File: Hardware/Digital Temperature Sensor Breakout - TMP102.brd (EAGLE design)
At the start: 15.2 x 15.2 mm, 13 parts, among them U1 TMP102-1:1

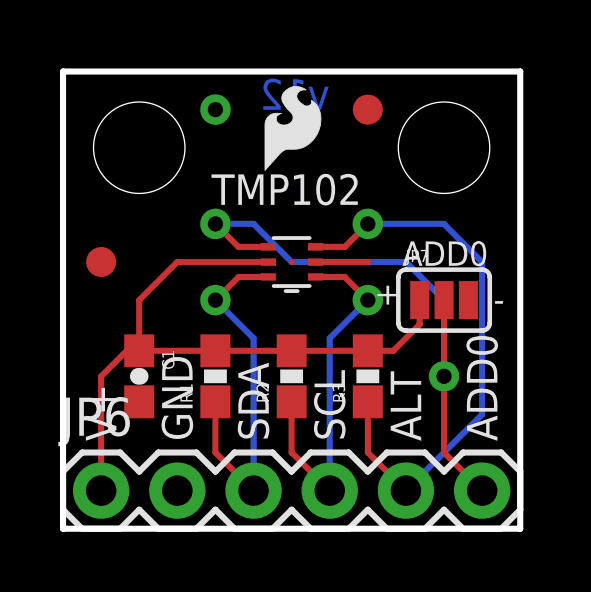
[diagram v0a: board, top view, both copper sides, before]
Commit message: Renamed board files
Renamed board files to match name of product on storefront. Also,
replaced main IC device with properly named variant from updated library
on github.
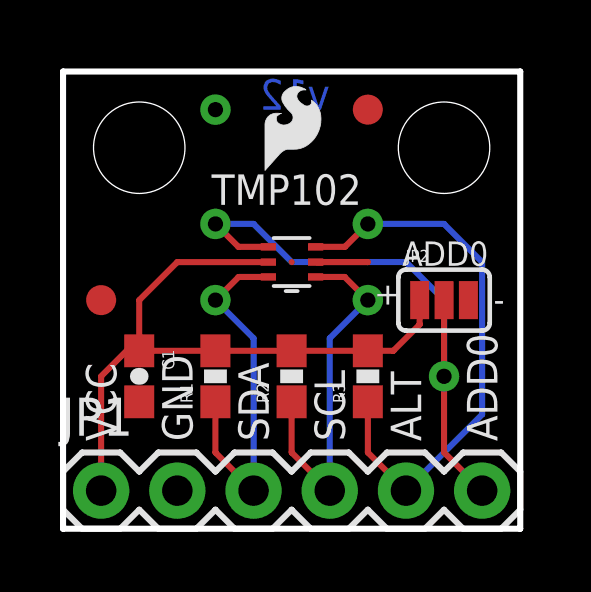
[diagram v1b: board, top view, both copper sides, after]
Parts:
- JP1: value STAND-OFFTIGHT -> (none); device SparkFun:STAND-OFF-TIGHT -> SparkFun:1X06
- JP2: value STAND-OFFTIGHT -> JUMPER-32-3; device SparkFun:STAND-OFF-TIGHT -> SparkFun:SJ_3_PASTE2&3
- JP6: value (none) -> STAND-OFFTIGHT; device SparkFun:1X06 -> SparkFun:STAND-OFF-TIGHT
- JP7: value JUMPER-32-3 -> STAND-OFFTIGHT; device SparkFun:SJ_3_PASTE2&3 -> SparkFun:STAND-OFF-TIGHT
- U1: value TMP102-1:1 -> TMP1021:1; device SparkFun:SOT563-2 -> SparkFun-Sensors:SOT563-2
- moved JP1 11.5 mm to (1.27, 1.27)
- moved JP6 11.5 mm to (2.54, 12.7)
- moved JP2 5.08 mm to (12.7, 7.62)
- moved JP7 5.08 mm to (12.7, 12.7)
- moved JP4 1.27 mm to (1.27, 7.62)
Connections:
- removed net V+: C1.1, JP6.1, JP7.1, R1.2, R2.2, R3.2, U1.5
- new net VCC: C1.1, JP1.1, JP2.1, R1.2, R2.2, R3.2, U1.5
- net ADD0: now also JP1.6, JP2.2; no longer JP6.6, JP7.2
- net ALERT: now also JP1.5; no longer JP6.5
- net GND: now also JP1.2, JP2.3; no longer JP6.2, JP7.3
- net SCL: now also JP1.4; no longer JP6.4
- net SDA: now also JP1.3; no longer JP6.3
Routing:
- net VCC: track 0.00 -> 22.5 mm
- net V+: track 22.5 -> 0.00 mm
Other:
- board text added: "VCC"
- board text removed: "V+"
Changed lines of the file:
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@@
 <text x="10.922" y="2.921" size="1.016" layer="22" font="vector" ratio="15" rot="MR90">ALT</text>
 <text x="5.842" y="2.921" size="1.016" layer="22" font="vector" ratio="15" rot="MR90">SDA</text>
-<text x="0.762" y="2.921" size="1.016" layer="22" font="vector" ratio="15" rot="MR90">V+</text>
+<text x="0.762" y="2.921" size="1.016" layer="22" font="vector" ratio="15" rot="MR90">VCC</text>
 <text x="13.462" y="2.921" size="1.016" layer="22" font="vector" ratio="15" rot="MR90">ADD0</text>
 <text x="4.953" y="10.795" size="1.016" layer="21" ratio="15">TMP102</text>
-<text x="8.89" y="13.97" size="1.016" layer="16" font="vector" ratio="15" rot="MR0">v12</text>
+<text x="8.89" y="13.97" size="1.016" layer="16" font="vector" ratio="20" rot="MR0">v12</text>
 <text x="11.176" y="7.366" size="0.8128" layer="21" font="vector" ratio="15" rot="R90">+</text>
 <text x="14.351" y="7.239" size="0.8128" layer="21" font="vector" ratio="15">-</text>
@@
 <text x="11.938" y="2.921" size="1.016" layer="21" font="vector" ratio="15" rot="R90">ALT</text>
 <text x="6.858" y="2.921" size="1.016" layer="21" font="vector" ratio="15" rot="R90">SDA</text>
-<text x="1.778" y="2.921" size="1.016" layer="21" font="vector" ratio="15" rot="R90">V+</text>
+<text x="1.778" y="2.921" size="1.016" layer="21" font="vector" ratio="15" rot="R90">VCC</text>
 <text x="14.478" y="2.921" size="1.016" layer="21" font="vector" ratio="15" rot="R90">ADD0</text>
 <text x="11.303" y="8.763" size="0.8128" layer="21" font="vector" ratio="15">ADD0</text>
@@
 <element name="C1" library="SparkFun" package="0603-CAP" value="0.1uF" x="2.54" y="5.08" rot="R270"/>
 <element name="JP3" library="SparkFun" package="SFE-LOGO-FLAME" value="LOGO-SFESK" x="6.731" y="11.938"/>
-<element name="JP4" library="SparkFun" package="FIDUCIAL-1X2" value="FIDUCIAL1X2" x="1.27" y="8.89"/>
+<element name="JP4" library="SparkFun" package="FIDUCIAL-1X2" value="FIDUCIAL1X2" x="1.27" y="7.62"/>
 <element name="JP5" library="SparkFun" package="FIDUCIAL-1X2" value="FIDUCIAL1X2" x="10.16" y="13.97"/>
-<element name="JP6" library="SparkFun" package="1X06" value="" x="1.27" y="1.27"/>
-<element name="JP1" library="SparkFun" package="STAND-OFF-TIGHT" value="STAND-OFFTIGHT" x="2.54" y="12.7"/>
-<element name="JP2" library="SparkFun" package="STAND-OFF-TIGHT" value="STAND-OFFTIGHT" x="12.7" y="12.7"/>
-<element name="JP7" library="SparkFun" package="SJ_3_PASTE2&amp;3" value="JUMPER-32-3" x="12.7" y="7.62"/>
-<element name="U1" library="SparkFun" package="SOT563-2" value="TMP102-1:1" x="7.62" y="8.89" rot="R180"/>
+<element name="JP1" library="SparkFun" package="1X06" value="" x="1.27" y="1.27"/>
+<element name="JP2" library="SparkFun" package="SJ_3_PASTE2&amp;3" value="JUMPER-32-3" x="12.7" y="7.62"/>
+<element name="U1" library="SparkFun-Sensors" package="SOT563-2" value="TMP1021:1" x="7.62" y="8.89" rot="R180"/>
 <element name="U$1" library="SparkFun" package="OSHW-LOGO-S" value="" x="7.62" y="8.89" rot="MR0"/>
+<element name="JP6" library="SparkFun" package="STAND-OFF-TIGHT" value="STAND-OFFTIGHT" x="2.54" y="12.7"/>
+<element name="JP7" library="SparkFun" package="STAND-OFF-TIGHT" value="STAND-OFFTIGHT" x="12.7" y="12.7"/>
 </elements>
 <signals>
@@
 <vertex x="0" y="0"/>
 </polygon>
-<contactref element="JP6" pad="2"/>
-<contactref element="JP7" pad="3"/>
+<contactref element="JP1" pad="2"/>
+<contactref element="JP2" pad="3"/>
 <contactref element="U1" pad="2"/>
 <polygon width="0.254" layer="1" isolate="0.3048">
@@
 </signal>
 <signal name="SCL">
-<contactref element="JP6" pad="4"/>
+<contactref element="JP1" pad="4"/>
 <contactref element="U1" pad="1"/>
 <contactref element="R2" pad="1"/>
@@
 </signal>
 <signal name="ALERT">
-<contactref element="JP6" pad="5"/>
+<contactref element="JP1" pad="5"/>
 <contactref element="U1" pad="3"/>
 <contactref element="R3" pad="1"/>
@@
 </signal>
 <signal name="SDA">
-<contactref element="JP6" pad="3"/>
+<contactref element="JP1" pad="3"/>
 <contactref element="U1" pad="6"/>
 <contactref element="R1" pad="1"/>
@@
 </signal>
 <signal name="ADD0">
-<contactref element="JP6" pad="6"/>
-<contactref element="JP7" pad="2"/>
+<contactref element="JP1" pad="6"/>
+<contactref element="JP2" pad="2"/>
 <contactref element="U1" pad="4"/>
 <wire x1="12.7" y1="2.54" x2="13.97" y2="1.27" width="0.2032" layer="1"/>
@@
 <wire x1="12.7" y1="2.54" x2="12.7" y2="5.08" width="0.2032" layer="1"/>
 </signal>
-<signal name="V+">
-<contactref element="JP6" pad="1"/>
-<contactref element="JP7" pad="1"/>
+<signal name="VCC">
+<contactref element="JP1" pad="1"/>
+<contactref element="JP2" pad="1"/>
 <contactref element="R3" pad="2"/>
 <contactref element="R2" pad="2"/>
@@
 </signal>
 </signals>
+<errors>
+</errors>
 </board>
 </drawing>

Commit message: Added better info in schematic
Added a change log, version number, default i2c address info, and
creative commons note to schematic.
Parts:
- added U$2: CREATIVE_COMMONS, SparkFun:CREATIVE_COMMONS
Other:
- board text added: "Kade Alexander Jensen"

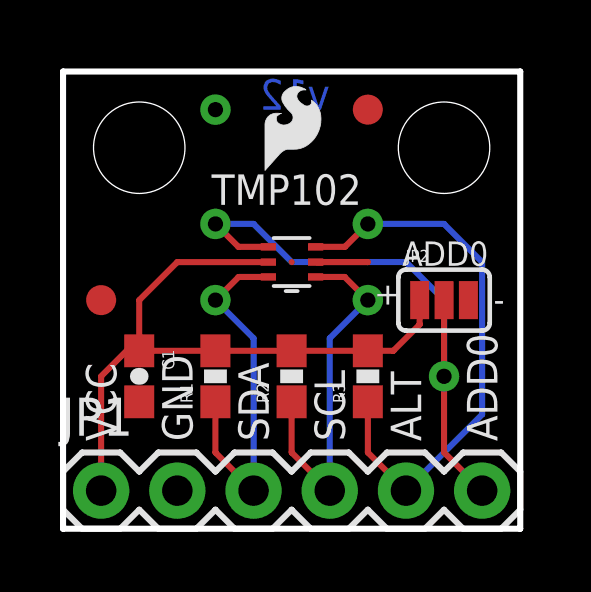
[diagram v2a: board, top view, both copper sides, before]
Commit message: Revision 13 changes
-Changed I2C address from 0x90 to 0x48.
-Changed I2C pull-up values to 4.7k
-Changed Alert pin pull-up to 4.7k
-Added I2C pull-up solder jumper
-Changed ADD0 pull-down jumper to 2-pad NC
-Added table of I2C addresses based on ADD0 connection.
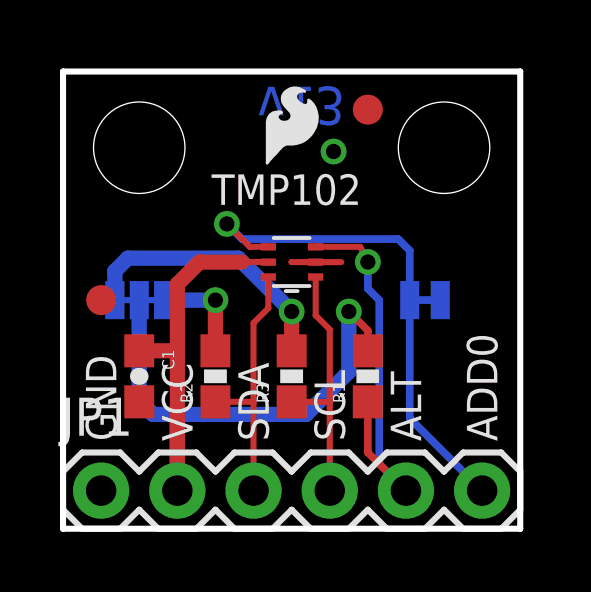
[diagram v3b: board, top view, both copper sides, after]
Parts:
- removed JP4: FIDUCIAL1X2, SparkFun:FIDUCIAL-1X2
- removed U$1: (no value), SparkFun:OSHW-LOGO-S
- added FRAME2: (no value), SparkFun-Aesthetics:CREATIVE_COMMONS
- added JP8: STAND-OFFTIGHT, SparkFun:STAND-OFF-TIGHT
- added LOGO2: SFE_LOGO_FLAME.1_INCH, SparkFun-Aesthetics:SFE_LOGO_FLAME_.1
- added LOGO3: OSHW-LOGOS, SparkFun-Aesthetics:OSHW-LOGO-S
- JP2: value JUMPER-32-3 -> (none); device SparkFun:SJ_3_PASTE2&3 -> SparkFun-Passives:PAD-JUMPER-3-3OF3_NC_BY_TRACE_YES_SILK_FULL_BOX
- JP3: value LOGO-SFESK -> ADD0; device SparkFun:SFE-LOGO-FLAME -> SparkFun-Passives:PAD-JUMPER-2-NC_BY_TRACE_YES_SILK
- JP6: value STAND-OFFTIGHT -> FIDUCIAL1X2; device SparkFun:STAND-OFF-TIGHT -> SparkFun:FIDUCIAL-1X2
- R1, R2, R3: value 1K -> 4.7k
- U$2: value CREATIVE_COMMONS -> REVISION; device SparkFun:CREATIVE_COMMONS -> SparkFun-Aesthetics:REVISION
- moved U$2 21.5 mm to (-10.8, -25.4)
- moved JP5 10.9 mm to (1.27, 7.62)
- moved JP2 10.2 mm to (2.54, 7.62), flipped to the bottom, turned to 180 degrees
- moved JP7 10.2 mm to (2.54, 12.7)
- moved JP6 7.73 mm to (10.2, 14.0)
- moved JP3 6.86 mm to (12.1, 7.62), flipped to the bottom, turned to 180 degrees
- moved R1 5.08 mm to (10.2, 5.08)
- moved R2 2.54 mm to (5.08, 5.08)
- moved R3 2.54 mm to (7.62, 5.08)
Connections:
- new net N$1: JP2.1, R3.2
- new net N$2: JP2.3, R2.2
- net ADD0: now also JP3.1; no longer JP2.2
- net ALERT: now also R1.1; no longer R3.1
- net GND: now also JP1.1, JP3.2; no longer JP1.2, JP2.3
- net SCL: now also R3.1; no longer R2.1
- net SDA: now also R2.1; no longer R1.1
- net VCC: now also JP1.2, JP2.2; no longer JP1.1, JP2.1, R2.2, R3.2
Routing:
- net N$1: track 0.00 -> 9.08 mm, vias 0 -> 1
- net VCC: track 22.5 -> 28.8 mm, vias 0 -> 1
- net ALERT: track 18.6 -> 13.7 mm
- net SDA: track 12.4 -> 8.60 mm, vias 1 -> 0
- net SCL: track 12.4 -> 8.59 mm, vias 1 -> 0
- net N$2: track 0.00 -> 3.42 mm, vias 0 -> 1
- net ADD0: track 20.2 -> 17.2 mm, vias 2 -> 1
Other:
- board text added: "Alex Wende"
- board text added: "I2C PU"
- board text removed: "+"
- board text removed: "v12"

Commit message: Applied Fixes from Design Review
-Moved traces on end of sensors to extend out the other way.
-Added note in schematic about using an external jumper to change I2C
address.
-Removed Kade's name from document layer.
-Added pull down resistor to prevent shorts with I2C address changes.
-Added unit of measurement on Measures layer.
-Changed measurements to use 0,0 as reference.
-Removed "-" on ADD0 jumper
-Changed VCC silk on top silk to voltage range.
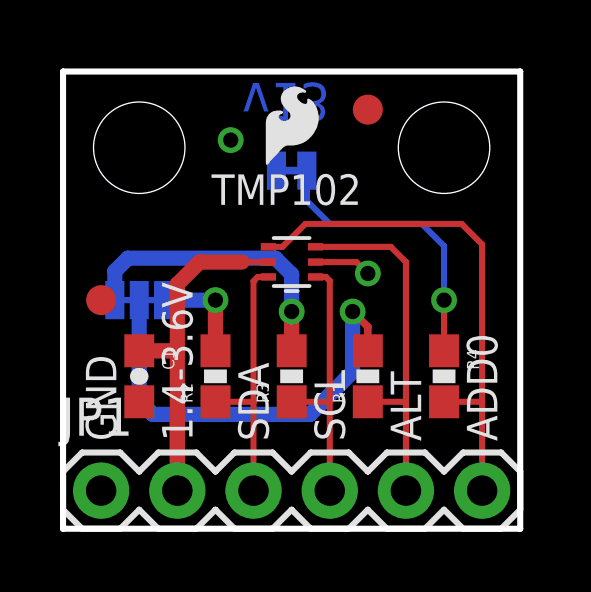
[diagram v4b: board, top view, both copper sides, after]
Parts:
- added R4: 10k, SparkFun:0603-RES
- R1: value 4.7k -> 10k
- moved JP3 6.20 mm to (7.62, 11.9), turned to 0 degrees
- moved LOGO3 5.09 mm to (12.7, 9.27)
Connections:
- new net N$3: JP3.1, R4.1
- net ADD0: now also R4.2; no longer JP3.1
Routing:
- net N$3: track 0.00 -> 9.70 mm, vias 0 -> 1
- net ALERT: track 13.7 -> 12.1 mm, vias 1 -> 0
- net N$1: track 9.08 -> 9.81 mm
- net GND: track 1.67 -> 1.90 mm, vias 1 -> 2
- net ADD0: vias 1 -> 0
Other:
- board text added: "1.4-3.6V"
- board text added: "Units are in Inches"
- board text removed: "-"
- board text removed: "Kade Alexander Jensen"

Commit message: QC Fixes
Updated parts with PROD_ID attributes
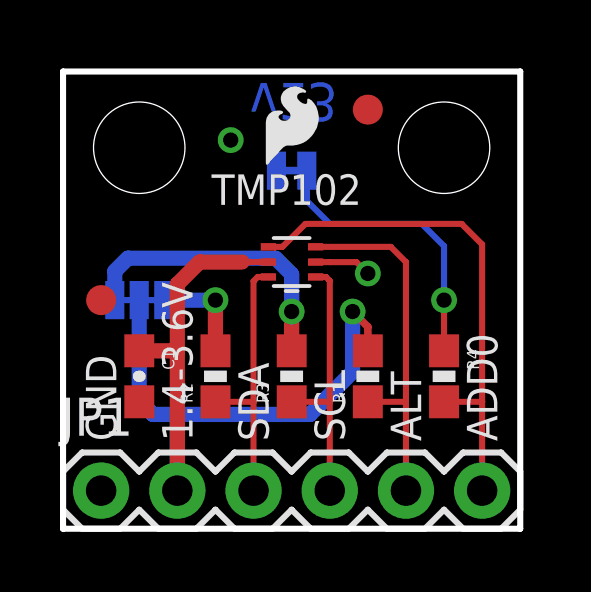
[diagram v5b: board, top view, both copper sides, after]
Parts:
- C1: device SparkFun:0603-CAP -> SparkFun-Capacitors:0603-CAP
- FRAME2: value (none) -> FRAME-LETTER
- R1, R4: value 10k -> 10K; device SparkFun:0603-RES -> SparkFun-Resistors:0603-RES
- R2, R3: value 4.7k -> 4.7K; device SparkFun:0603-RES -> SparkFun-Resistors:0603-RES
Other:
- board text added: "Kade Alexander Jensen"
- board text added: "v13"
